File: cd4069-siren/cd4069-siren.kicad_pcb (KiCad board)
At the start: 2 copper layers, 35.1 x 39.4 mm, 21 parts

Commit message: Reviewed schematics and boards
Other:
- board text added: "A to na warstwie F.Cu"
- board text added: "To może iść pod piezo1"
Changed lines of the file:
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@@
+    (effects (font (size 1 1) (thickness 0.15)) (justify left bottom))
+  )
+  (gr_text "To może iść pod piezo1" (at 113.025 72.275) (layer "User.8")
+    (effects (font (size 1 1) (thickness 0.15)) (justify left bottom))
+  )
+  (gr_text "A to na warstwie F.Cu" (at 109.5 73.625) (layer "User.8")
     (effects (font (size 1 1) (thickness 0.15)) (justify left bottom))
   )

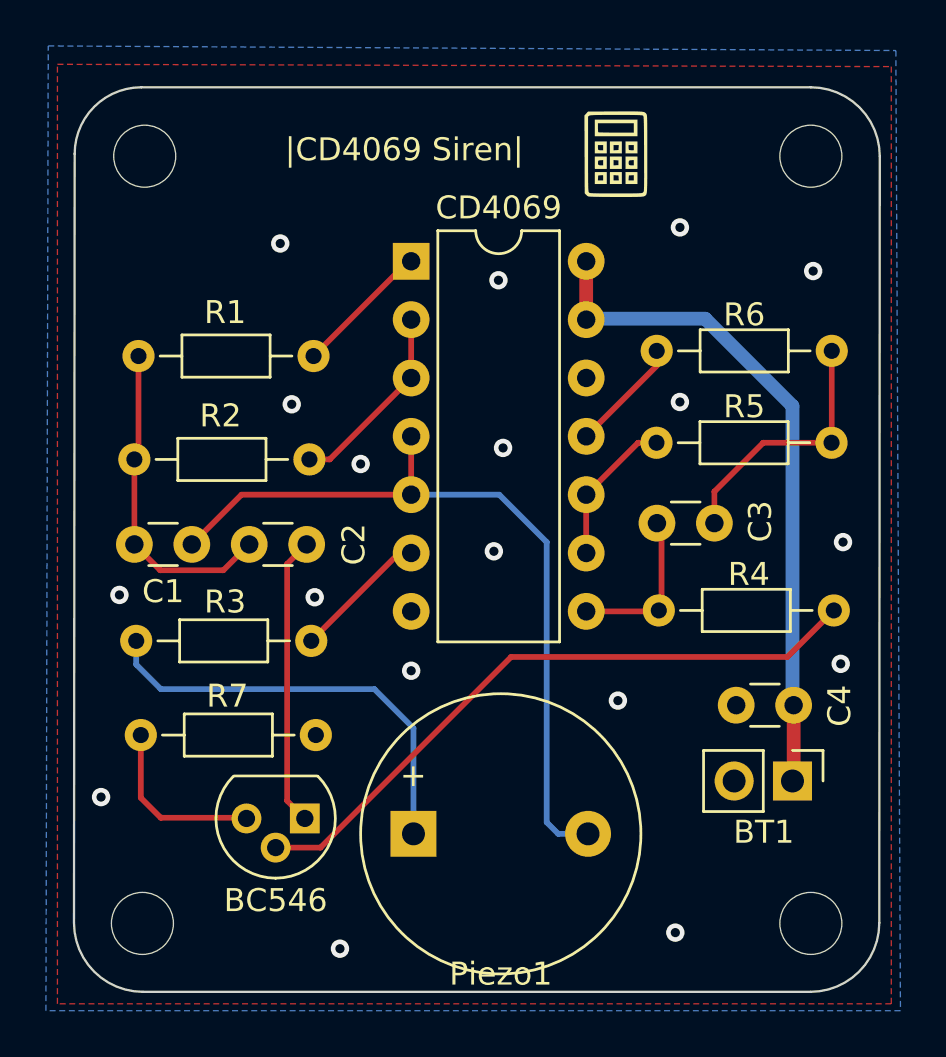
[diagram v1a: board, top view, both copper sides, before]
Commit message: project 7 / cd4069 siren / improved schematics and pcb after review
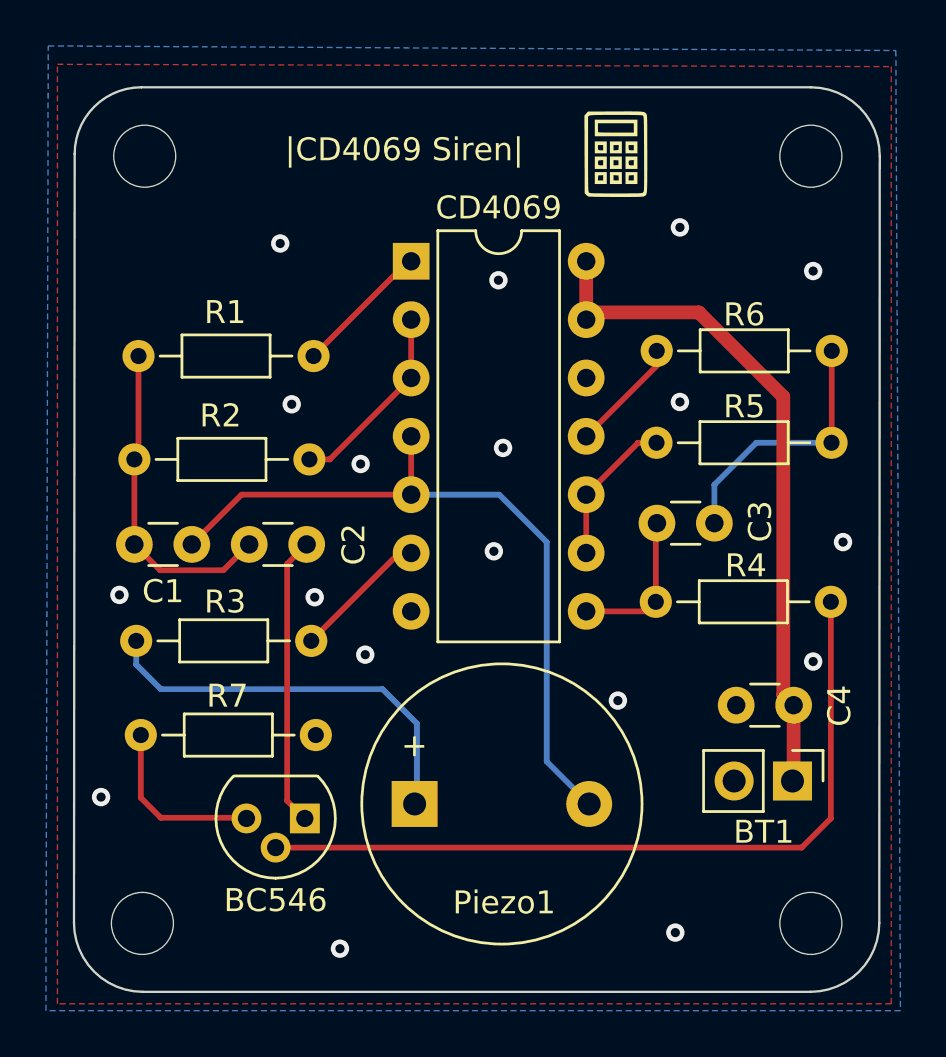
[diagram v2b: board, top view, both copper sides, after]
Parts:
- moved Piezo1 1.30 mm to (103.8, 78.6)
- moved R4 0.40 mm to (114.2, 69.8)
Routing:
- net Net-(BC546-B): track 28.6 -> 34.1 mm
- net /I0: track 33.9 -> 31.9 mm
- net Net-(Piezo1-Pad1): track 18.8 -> 17.9 mm
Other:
- board text removed: "A to na warstwie F.Cu"
- board text removed: "To może iść pod piezo1"
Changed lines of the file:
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@@
   )
   (footprint "Resistor_THT:R_Axial_DIN0204_L3.6mm_D1.6mm_P7.62mm_Horizontal" (layer "F.Cu")
-    (at 114.38 70.175)
+    (at 114.25 69.8)
     (descr "Resistor, Axial_DIN0204 series, Axial, Horizontal, pin pitch=7.62mm, 0.167W, length*diameter=3.6*1.6mm^2, http://cdn-reichelt.de/documents/datenblatt/B400/1_4W%23YAG.pdf")
     (tags "Resistor Axial_DIN0204 series Axial Horizontal pin pitch 7.62mm 0.167W length 3.6mm diameter 1.6mm")
@@
         (effects (font (size 1 1) (thickness 0.15)))
     )
-    (fp_text value "4069" (at 3.81 17.57) (layer "F.Fab")
+    (fp_text value "4069" (at 3.9 5.425) (layer "F.Fab")
         (effects (font (size 1 1) (thickness 0.15)))
     )
@@
   )
   (footprint "Buzzer_Beeper:Buzzer_12x9.5RM7.6" (layer "F.Cu")
-    (at 103.7 79.9)
+    (at 103.75 78.6)
     (descr "Generic Buzzer, D12mm height 9.5mm with RM7.6mm")
     (tags "buzzer")
@@
     (property "ki_keywords" "crystal speaker ultrasonic transducer")
     (attr through_hole)
-    (fp_text reference "Piezo1" (at 3.8 6.1) (layer "F.SilkS")
+    (fp_text reference "Piezo1" (at 3.9 4.3) (layer "F.SilkS")
         (effects (font (size 1 1) (thickness 0.15)))
     )
@@
     (effects (font (size 1 1) (thickness 0.15)) (justify left bottom))
   )
-  (gr_text "To może iść pod piezo1" (at 113.025 72.275) (layer "User.8")
-    (effects (font (size 1 1) (thickness 0.15)) (justify left bottom))
-  )
-  (gr_text "A to na warstwie F.Cu" (at 109.5 73.625) (layer "User.8")
-    (effects (font (size 1 1) (thickness 0.15)) (justify left bottom))
-  )
   (segment (start 98.2 78.46) (end 98.97 79.23) (width 0.25) (layer "F.Cu") (net 1))
   (segment (start 98.2 68.15) (end 98.2 78.46) (width 0.25) (layer "F.Cu") (net 1))
   (segment (start 99.05 67.3) (end 98.2 68.15) (width 0.25) (layer "F.Cu") (net 1))
-  (segment (start 119.975 72.2) (end 107.95 72.2) (width 0.25) (layer "F.Cu") (net 2))
-  (segment (start 107.95 72.2) (end 99.65 80.5) (width 0.25) (layer "F.Cu") (net 2))
-  (segment (start 122 70.175) (end 119.975 72.2) (width 0.25) (layer "F.Cu") (net 2))
-  (segment (start 99.65 80.5) (end 97.7 80.5) (width 0.25) (layer "F.Cu") (net 2))
+  (segment (start 120.6 80.5) (end 121.87 79.23) (width 0.25) (layer "F.Cu") (net 2))
+  (segment (start 121.87 79.23) (end 121.87 69.8) (width 0.25) (layer "F.Cu") (net 2))
+  (segment (start 97.7 80.5) (end 120.6 80.5) (width 0.25) (layer "F.Cu") (net 2))
   (segment (start 91.83 78.33) (end 92.7 79.2) (width 0.25) (layer "F.Cu") (net 3))
   (segment (start 91.83 75.6) (end 91.83 78.33) (width 0.25) (layer "F.Cu") (net 3))
@@
   (segment (start 96.4 79.2) (end 96.43 79.23) (width 0.25) (layer "F.Cu") (net 3))
   (segment (start 120.25 77.55) (end 120.2 77.6) (width 0.6) (layer "F.Cu") (net 4))
+  (segment (start 119.8 73.85) (end 120.2 74.25) (width 0.6) (layer "F.Cu") (net 4))
+  (segment (start 111.26 57.475) (end 111.535 57.2) (width 0.6) (layer "F.Cu") (net 4))
   (segment (start 111.22 57.515) (end 111.22 54.975) (width 0.6) (layer "F.Cu") (net 4))
+  (segment (start 119.8 60.875) (end 119.8 73.85) (width 0.6) (layer "F.Cu") (net 4))
+  (segment (start 116.125 57.2) (end 119.8 60.875) (width 0.6) (layer "F.Cu") (net 4))
   (segment (start 120.25 74.3) (end 120.25 77.55) (width 0.6) (layer "F.Cu") (net 4))
-  (segment (start 120.2 61.275) (end 120.2 74.25) (width 0.6) (layer "B.Cu") (net 4))
-  (segment (start 111.26 57.475) (end 116.4 57.475) (width 0.6) (layer "B.Cu") (net 4))
-  (segment (start 116.4 57.475) (end 120.2 61.275) (width 0.6) (layer "B.Cu") (net 4))
+  (segment (start 111.535 57.2) (end 116.125 57.2) (width 0.6) (layer "F.Cu") (net 4))
   (segment (start 111.22 57.515) (end 111.26 57.475) (width 0.6) (layer "B.Cu") (net 4))
   (segment (start 120.2 74.25) (end 120.25 74.3) (width 0.6) (layer "B.Cu") (net 4))
@@
   (via (at 90.1 78.3) (size 0.8) (drill 0.4) (layers "F.Cu" "B.Cu") (free) (net 5))
   (via (at 122.4 67.2) (size 0.8) (drill 0.4) (layers "F.Cu" "B.Cu") (free) (net 5))
-  (via (at 122.3 72.5) (size 0.8) (drill 0.4) (layers "F.Cu" "B.Cu") (free) (net 5))
+  (via (at 121.1 72.4) (size 0.8) (drill 0.4) (layers "F.Cu" "B.Cu") (free) (net 5))
   (via (at 107.2 67.6) (size 0.8) (drill 0.4) (layers "F.Cu" "B.Cu") (free) (net 5))
   (via (at 97.9 54.2) (size 0.8) (drill 0.4) (layers "F.Cu" "B.Cu") (free) (net 5))
@@
   (via (at 115.3 53.5) (size 0.8) (drill 0.4) (layers "F.Cu" "B.Cu") (free) (net 5))
   (via (at 100.5 84.9) (size 0.8) (drill 0.4) (layers "F.Cu" "B.Cu") (free) (net 5))
-  (via (at 103.6 72.8) (size 0.8) (drill 0.4) (layers "F.Cu" "B.Cu") (free) (net 5))
+  (via (at 101.6 72.1) (size 0.8) (drill 0.4) (layers "F.Cu" "B.Cu") (free) (net 5))
   (segment (start 94.05 67.3) (end 96.215 65.135) (width 0.25) (layer "F.Cu") (net 6))
   (segment (start 103.6 62.595) (end 103.6 65.135) (width 0.25) (layer "F.Cu") (net 6))
   (segment (start 96.215 65.135) (end 103.6 65.135) (width 0.25) (layer "F.Cu") (net 6))
-  (segment (start 111.3 79.9) (end 110 79.9) (width 0.25) (layer "B.Cu") (net 6))
+  (segment (start 109.5 76.75) (end 109.5 67.2) (width 0.25) (layer "B.Cu") (net 6))
+  (segment (start 111.35 78.6) (end 109.5 76.75) (width 0.25) (layer "B.Cu") (net 6))
   (segment (start 107.435 65.135) (end 103.6 65.135) (width 0.25) (layer "B.Cu") (net 6))
   (segment (start 109.5 67.2) (end 107.435 65.135) (width 0.25) (layer "B.Cu") (net 6))
-  (segment (start 109.5 79.4) (end 109.5 67.2) (width 0.25) (layer "B.Cu") (net 6))
-  (segment (start 110 79.9) (end 109.5 79.4) (width 0.25) (layer "B.Cu") (net 6))
   (segment (start 91.55 63.6) (end 91.55 67.3) (width 0.25) (layer "F.Cu") (net 7))
   (segment (start 92.675 68.425) (end 95.425 68.425) (width 0.25) (layer "F.Cu") (net 7))
@@
   (segment (start 91.73 59.1) (end 91.73 63.42) (width 0.25) (layer "F.Cu") (net 7))
   (segment (start 91.55 67.3) (end 92.675 68.425) (width 0.25) (layer "F.Cu") (net 7))
-  (segment (start 114.5 66.575) (end 114.5 70.055) (width 0.25) (layer "F.Cu") (net 8))
-  (segment (start 114.34 70.215) (end 114.38 70.175) (width 0.25) (layer "F.Cu") (net 8))
-  (segment (start 111.22 70.215) (end 114.34 70.215) (width 0.25) (layer "F.Cu") (net 8))
-  (segment (start 114.5 70.055) (end 114.38 70.175) (width 0.25) (layer "F.Cu") (net 8))
-  (segment (start 114.3 66.375) (end 114.5 66.575) (width 0.25) (layer "F.Cu") (net 8))
+  (segment (start 114.3 66.85) (end 114.3 66.375) (width 0.25) (layer "F.Cu") (net 8))
+  (segment (start 111.22 70.215) (end 113.835 70.215) (width 0.25) (layer "F.Cu") (net 8))
+  (segment (start 111.22 70.215) (end 111.22 69.93) (width 0.25) (layer "F.Cu") (net 8))
+  (segment (start 113.835 70.215) (end 114.25 69.8) (width 0.25) (layer "F.Cu") (net 8))
+  (segment (start 114.25 69.8) (end 114.25 66.425) (width 0.25) (layer "F.Cu") (net 8))
+  (segment (start 114.25 66.425) (end 114.3 66.375) (width 0.25) (layer "F.Cu") (net 8))
+  (segment (start 111.21 70.225) (end 111.22 70.215) (width 0.25) (layer "F.Cu") (net 8))
   (segment (start 121.91 58.675) (end 121.91 62.865) (width 0.25) (layer "F.Cu") (net 9))
-  (segment (start 118.925 62.875) (end 121.9 62.875) (width 0.25) (layer "F.Cu") (net 9))
   (segment (start 121.91 62.865) (end 121.9 62.875) (width 0.25) (layer "F.Cu") (net 9))
-  (segment (start 116.8 65) (end 118.925 62.875) (width 0.25) (layer "F.Cu") (net 9))
-  (segment (start 116.8 66.375) (end 116.8 65) (width 0.25) (layer "F.Cu") (net 9))
+  (segment (start 116.8 64.7) (end 116.8 66.375) (width 0.25) (layer "B.Cu") (net 9))
+  (segment (start 121.9 62.875) (end 118.625 62.875) (width 0.25) (layer "B.Cu") (net 9))
+  (segment (start 118.625 62.875) (end 116.8 64.7) (width 0.25) (layer "B.Cu") (net 9))
   (segment (start 91.63 72.53) (end 92.7 73.6) (width 0.25) (layer "B.Cu") (net 10))
-  (segment (start 103.7 75.3) (end 103.7 79.9) (width 0.25) (layer "B.Cu") (net 10))
-  (segment (start 92.7 73.6) (end 102 73.6) (width 0.25) (layer "B.Cu") (net 10))
+  (segment (start 103.85 78.5) (end 103.75 78.6) (width 0.25) (layer "B.Cu") (net 10))
+  (segment (start 102.35 73.6) (end 103.85 75.1) (width 0.25) (layer "B.Cu") (net 10))
+  (segment (start 103.85 75.1) (end 103.85 78.5) (width 0.25) (layer "B.Cu") (net 10))
+  (segment (start 92.7 73.6) (end 102.35 73.6) (width 0.25) (layer "B.Cu") (net 10))
   (segment (start 91.63 71.5) (end 91.63 72.53) (width 0.25) (layer "B.Cu") (net 10))
-  (segment (start 102 73.6) (end 103.7 75.3) (width 0.25) (layer "B.Cu") (net 10))
   (segment (start 103.475 54.975) (end 103.6 54.975) (width 0.25) (layer "F.Cu") (net 11))
   (segment (start 99.35 59.1) (end 103.475 54.975) (width 0.25) (layer "F.Cu") (net 11))
